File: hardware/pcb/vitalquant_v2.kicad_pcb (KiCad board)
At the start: 8 copper layers, 55.6 x 81 mm, 303 parts, among them J1 USB-C, J10 Optical tail pads, J11 Sweat site, J12 FH12-14S, J13 MX ECG pads, J2 LiPo pads, J3 FSR pads, J5 ECG pads, J6 EDA pads, J7 Chest bioZ, J8 TC2030, J9 I2C tail pads, Q1 CSD13380F3T, Q2 CSD13380F3T, Q3 BC847BS,115, Q4 CSD13380F3T, Q6 AO3401A, SW1 TS-1088, SW2 TS-1088, U1 ESP32-S3-MINI-1-N4R2, U1 ESP32-S3-WROOM-1-N16R8, U10 AS7341-DLGM, U11 TMP117AIDRVR, U12 MLX90632SLD-DCB-100-SP, U13 BME280, U14 LSM6DSV80XTR, U15 TPS61240YFFR, U16 SFH 7072, U17 MAX17048G+T10, U18 W25Q512JVEIQ, U19 TCA6408ARSVR, U2 BQ25170DSGR, U20 TMP117AIDRVR, U21 USBLC6-2SC6, U22 MAX86141ENP+, U23 SHT45-AD1B, U24 RV-3028-C7, U25 IM69D130, U26 SN74AXC2T245RSWR, U3 TPS63802DLAR, U4 TPS7A2018PDBVR, U5 CP2102N-A02-GQFN28R, U6 AFE4900YZR, U7 AD5940BCBZ-RL7, U8 ADS1292RIRSMT, U9 PCA9306DCUR

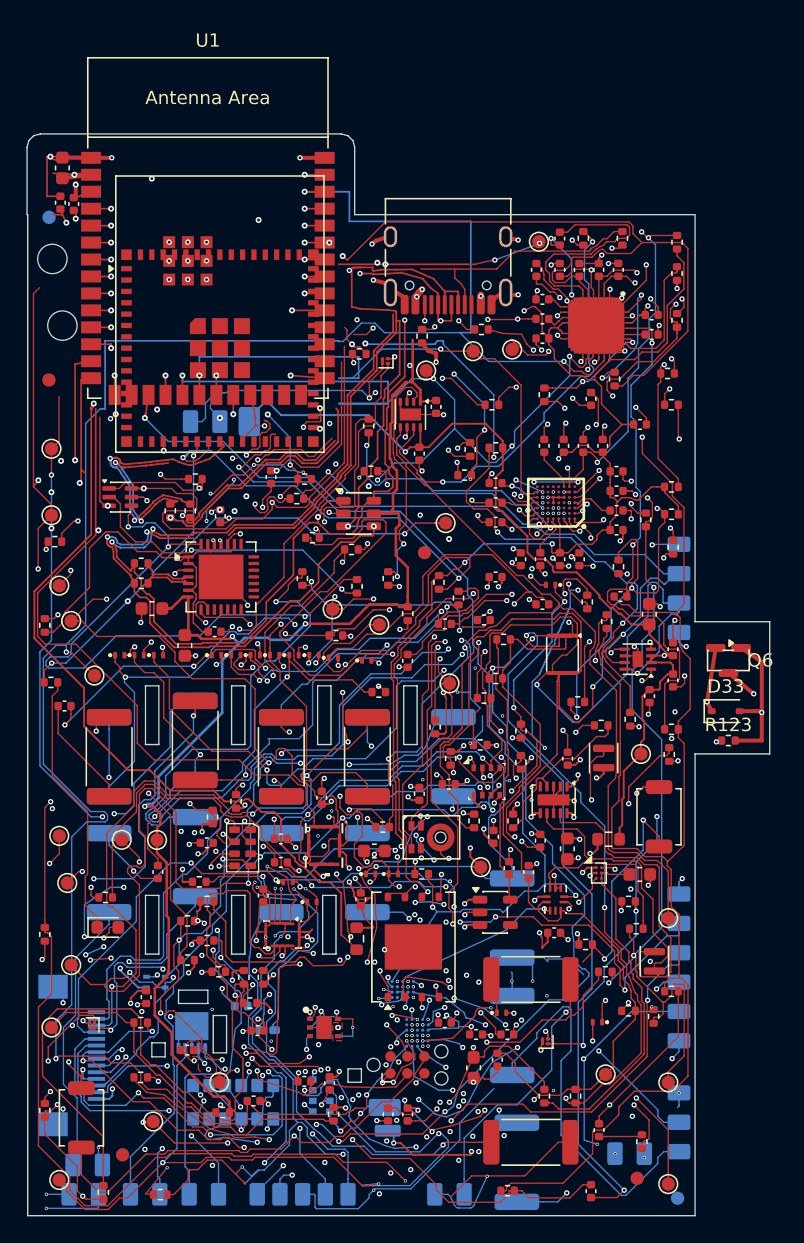
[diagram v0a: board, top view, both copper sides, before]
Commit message: hw(pcb): fix_v24 board — BOM fields/flags only, copper identical to fix_v23
BOM v24 revision on the fix_v23 design (KiCad 10.0.4):
- U14 LSM6DSV80XTR -> LSM6DSV320XTR (LCSC C26633007), same LGA-14 land
- D10 -> Nichia NF2W757G-F1, consigned (LCSC blank) — footprint is drawn
  for the Nichia part; the Cree JB3030 did not match the land
- J12 / U24 / U25 fitted again and back in BOM_JLC / CPL_JLC
- Dead MX-ECG chain D29 / D30 / R118 / R119 marked DNP (netlist-proven:
  MX_ECG_INP/INM reach only J13-DNP and GND; U22 MAX86141 has no ECG in)
- J2-J11 copper pad footprints excluded from BOM and position files
- ~30 LCSC corrections + verified swaps (U8 ADS1292RIRSMR C456281,
  U12 MLX90632-RE C17235844, 7x 470n Y5V->X5R C47339, R-series fixes)

Schematic fields (Value/MPN/LCSC/Manufacturer), DNP and in_bom /
exclude-from-pos flags synced into the matching PCB footprint properties
and attributes — add-only, existing flags preserved. No copper, track,
via, zone, footprint-geometry, position, Edge.Cuts or drill changes;
all 16 gerber layers byte-identical to fix_v23, drills identical.

Also restores the fix_v23 design on main: the firmware merge resolution
("feature branch wins") had reverted the board to the fixv19d revision
and left unresolved conflict markers in the schematic. U1 stays
ESP32-S3-WROOM-1-N16R8 as in fix_v23/v24; the MINI footprint remains in
vitalquant.pretty pending the owner's MINI-vs-WROOM call.

DRC --severity-error --schematic-parity (fix_v19 rules + narrow
.kicad_dru): 0/0/0/0. ERC --severity-error: 0. Verified on the rebranded
files in this commit.

Generated with [Devin](https://devin.ai)

Co-Authored-By: Devin <158243242+devin-ai-integration[bot]@users.noreply.github.com>
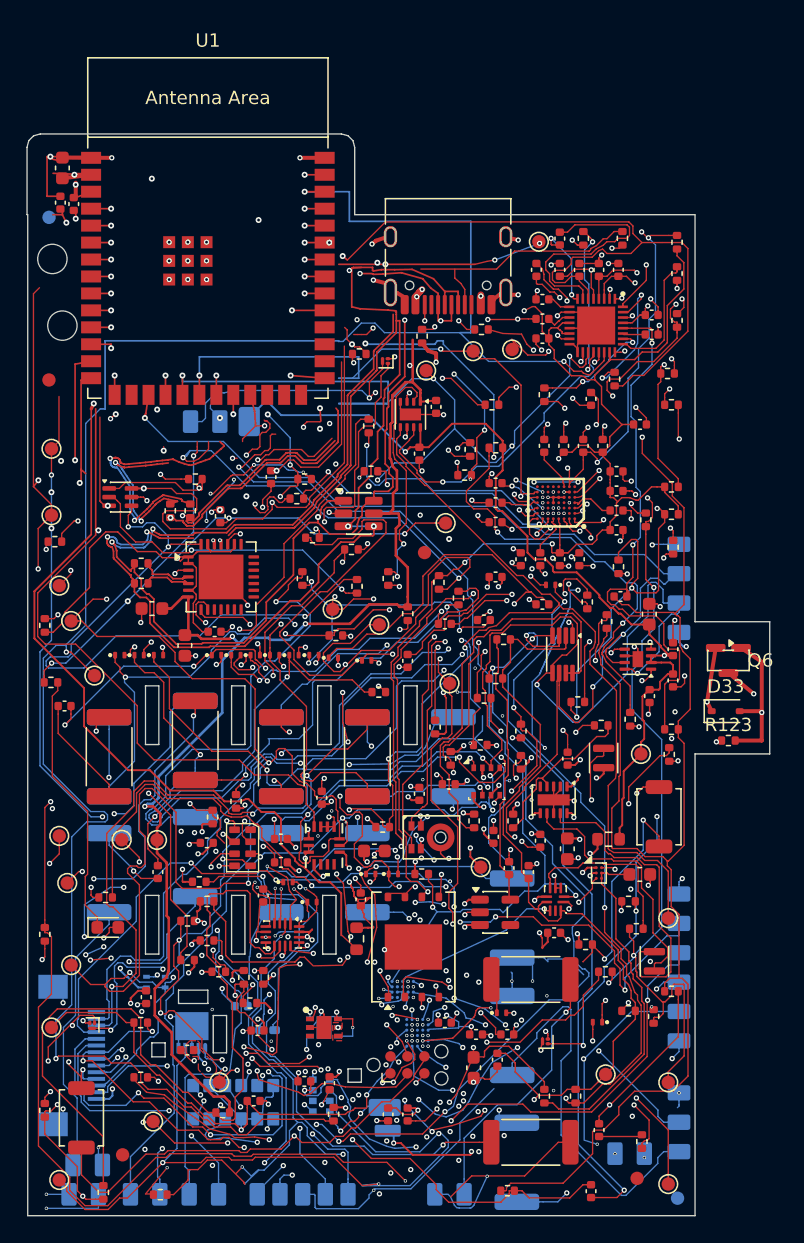
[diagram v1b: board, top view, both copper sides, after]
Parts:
- removed the U1 at (12.4, -0.50)
- U12: value MLX90632SLD-DCB-100-SP -> MLX90632SLD-DCB-100-RE
- U14: value LSM6DSV80XTR -> LSM6DSV320XTR
- U8: value ADS1292RIRSMT -> ADS1292RIRSMR
